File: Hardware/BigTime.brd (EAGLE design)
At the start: 43.2 x 43.2 mm, 14 parts, among them U1 ATMEGA328P_PDIP_EZ, Y1 32.768kHz

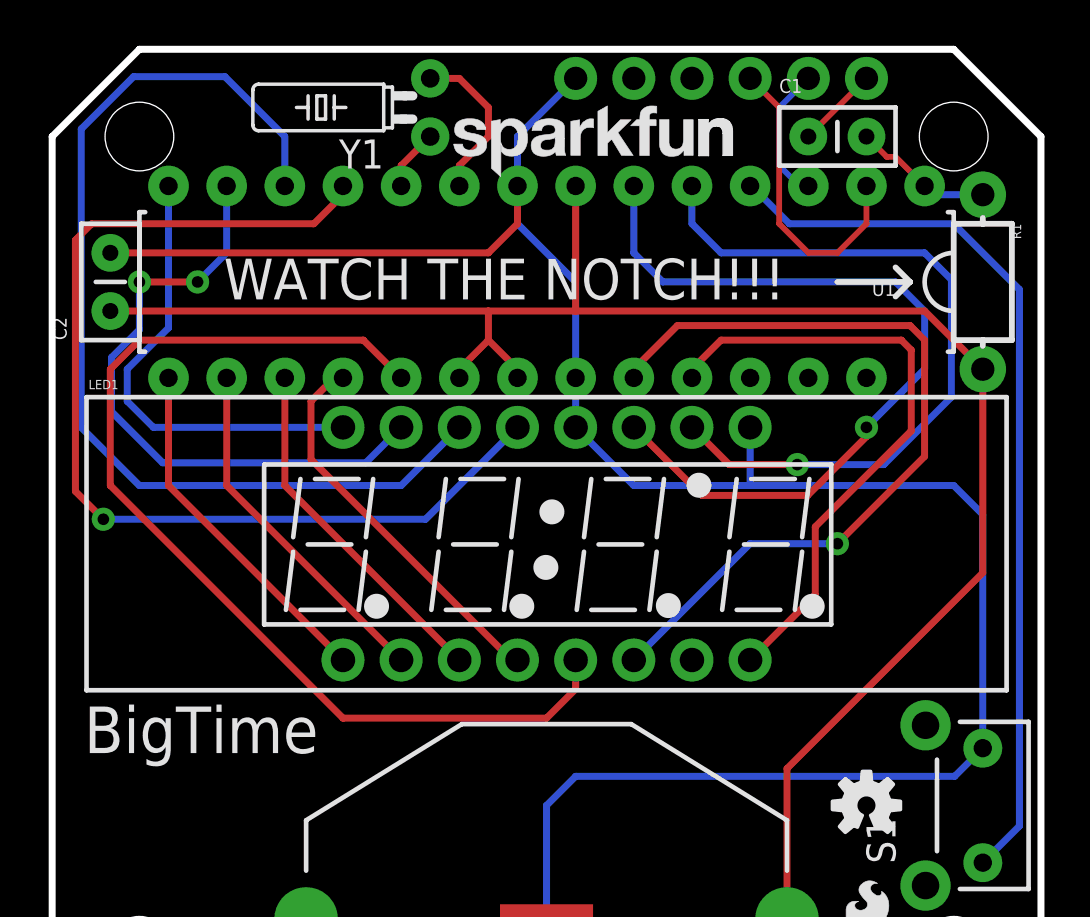
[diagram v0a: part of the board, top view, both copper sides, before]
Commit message: replace LED with bubble display
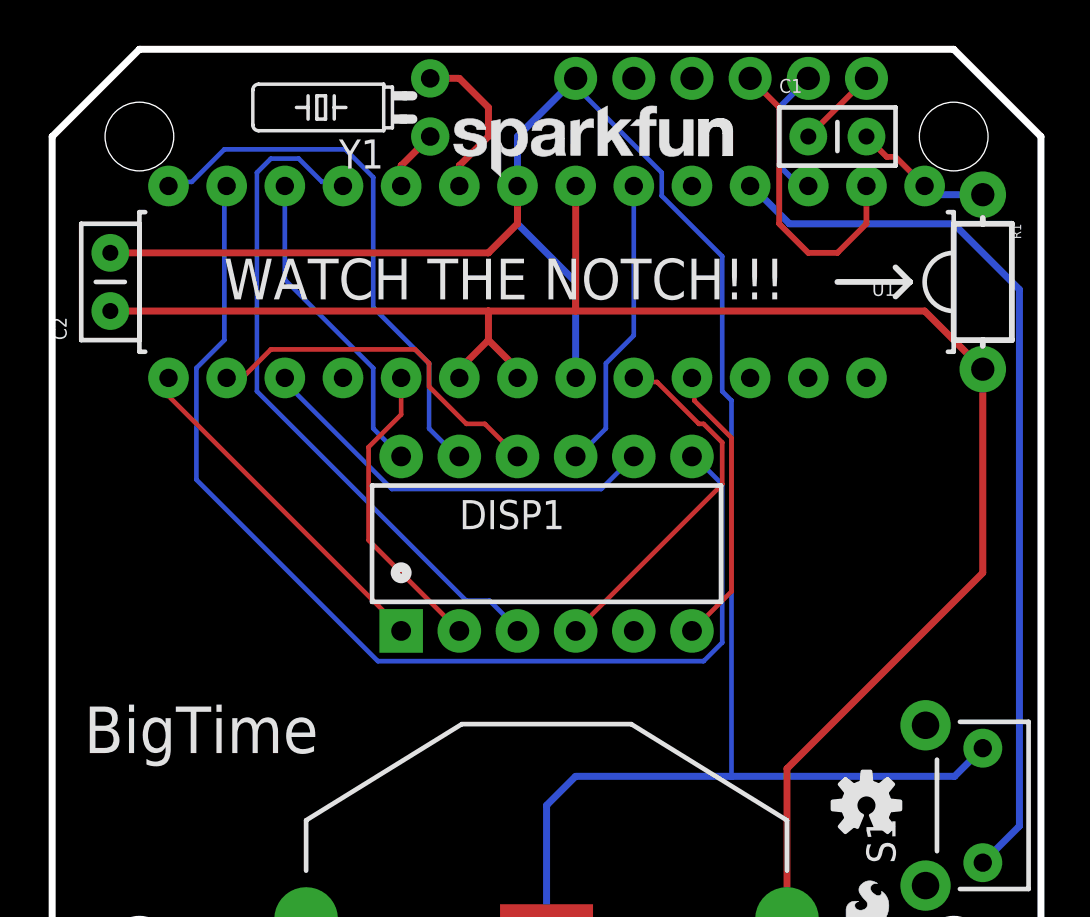
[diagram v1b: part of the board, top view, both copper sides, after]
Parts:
- removed LED1: 7-SEGMENT-4DIGIT-YOUNGSUNKIT, Testing:7-SEGMENT-4DIGIT-YOUNGSUN-KIT
- added DISP1: 7-SEGMENT-4DIGIT-COUNTER-HP-BUBBLE, SparkFun-Displays:DIL12
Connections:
- net A: now also DISP1.12; no longer LED1.14
- net AMPM: no longer LED1.10
- net B: now also DISP1.11; no longer LED1.16
- net C: now also DISP1.3; no longer LED1.13
- net COL: no longer LED1.4
- net D: now also DISP1.8; no longer LED1.3
- net DIG1: now also DISP1.1; no longer LED1.1
- net DIG2: now also DISP1.10; no longer LED1.2
- net DIG3: now also DISP1.4; no longer LED1.6
- net DIG4: now also DISP1.6; no longer LED1.8
- net DP: now also DISP1.5; no longer LED1.7
- net E: now also DISP1.2; no longer LED1.5
- net F: now also DISP1.9; no longer LED1.11
- net G: now also DISP1.7; no longer LED1.15
- net GND: no longer LED1.12, LED1.9
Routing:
- net AMPM: track 32.3 -> 0.00 mm, vias 1 -> 0
- net E: track 45.3 -> 13.3 mm
- net A: track 44.7 -> 13.9 mm
- net F: track 35.7 -> 12.9 mm, vias 1 -> 0
- net G: track 27.6 -> 48.7 mm, vias 2 -> 0
- net DIG3: track 35.6 -> 16.0 mm, vias 1 -> 0
- net COL: track 17.0 -> 0.00 mm
- net C: track 45.3 -> 29.9 mm, vias 1 -> 0
- net DIG4: track 27.1 -> 12.5 mm
- net B: track 20.0 -> 24.0 mm
- net D: track 15.5 -> 17.9 mm
- net GND: track 95.8 -> 95.0 mm

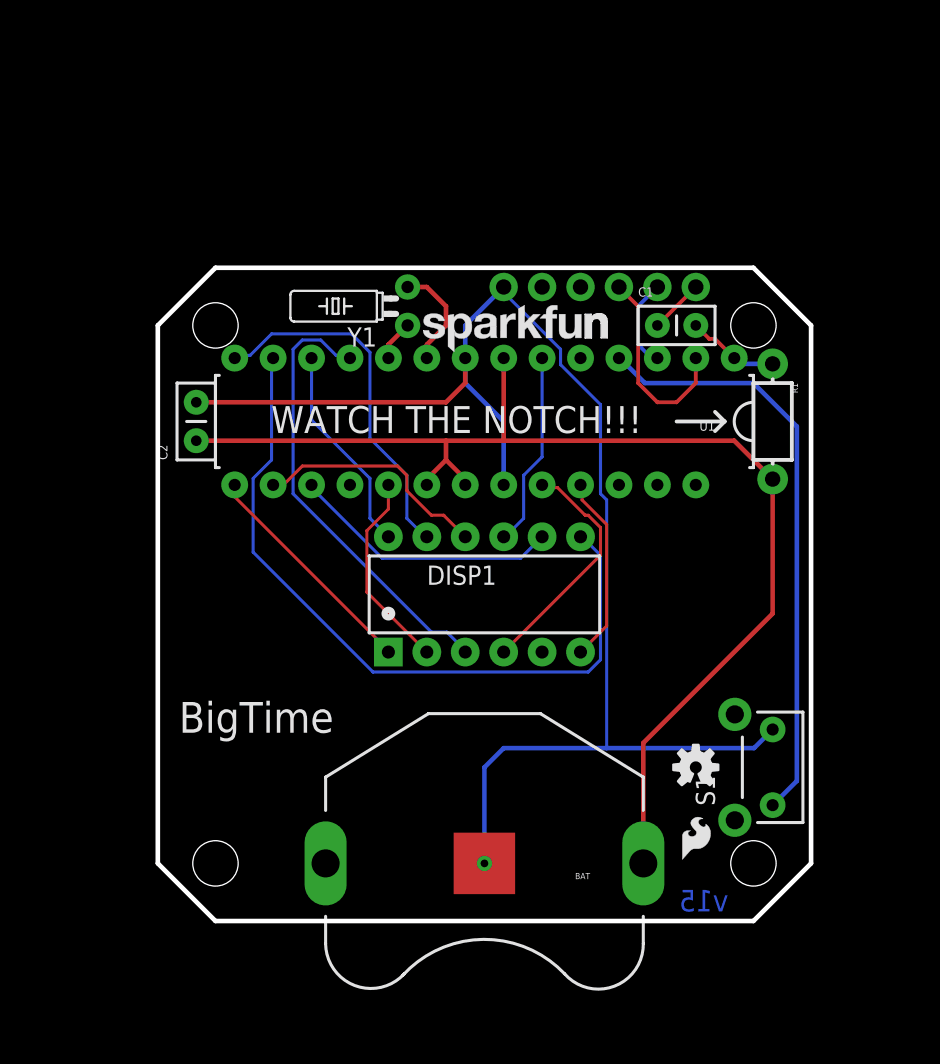
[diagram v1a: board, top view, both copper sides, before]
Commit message: add set button, reroute pub
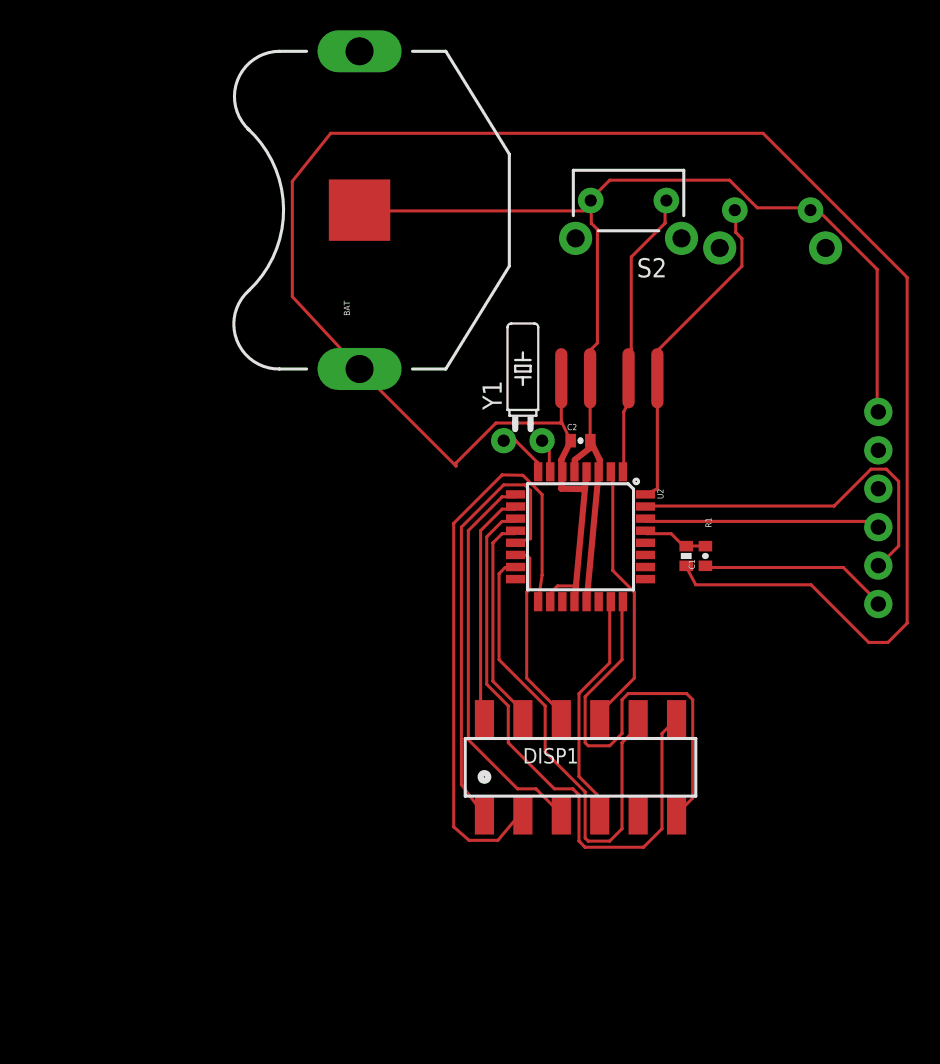
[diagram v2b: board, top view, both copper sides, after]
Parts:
- removed U$1: LOGO-SFESK, SparkFun:SFE-LOGO-FLAME
- removed U$3: LOGO-SFENEW, SparkFun:SFE-NEW-WEBLOGO
- removed U$4: OSHW-LOGOS, SparkFun:OSHW-LOGO-S
- removed U$5: LOGO-SFENW2, SparkFun:SFE-NEW-WEB
- removed U1: ATMEGA328P_PDIP_EZ, SparkFun-DigitalIC:DIL28-EZ
- added S2: BUTTON, SparkFun-Electromechanical:TACTILE-PTH-SIDEEZ
- added U2: ATMEGA328P_TQFP, SparkFun-DigitalIC:TQFP32-08
- C1, C2: device SparkFun-Passives:CAP-PTH-SMALLEZ -> SparkFun-Passives:0402-CAP
- DISP1: value 7-SEGMENT-4DIGIT-COUNTER-HP-BUBBLE -> 7-SEGMENT-4DIGIT-COUNTER-HP-BUBBLE-SM; device SparkFun-Displays:DIL12 -> SparkFun-Displays:DIL12_SM
- R1: device SparkFun-Passives:AXIAL-0.3-KIT -> SparkFun-Passives:0402-RES
- moved BAT 44.0 mm to (13.3, 47.0), turned to 90 degrees
- moved S1 36.8 mm to (40.6, 47.0), flipped to the bottom, turned to 180 degrees
- moved C2 25.4 mm to (27.9, 31.8), turned to 0 degrees
- moved JP1 24.2 mm to (47.6, 21.0), turned to 90 degrees
- moved C1 15.6 mm to (36.2, 24.1), turned to 90 degrees
- moved DISP1 13.1 mm to (27.9, 10.2)
- moved Y1 11.7 mm to (24.1, 31.8), turned to 0 degrees
- moved R1 10.6 mm to (34.9, 24.1)
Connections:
- removed net AMPM: U1.5
- new net SET: S2.1, U2.1
- net A: now also U2.10; no longer U1.12
- net B: now also U2.12; no longer U1.14
- net BTN: now also U2.32; no longer U1.4
- net C: now also U2.9; no longer U1.11
- net COL: now also U2.16; no longer U1.18
- net D: now also U2.15; no longer U1.17
- net DIG1: now also U2.13; no longer U1.15
- net DIG2: now also U2.14; no longer U1.16
- net DIG3: now also U2.23; no longer U1.23
- net DIG4: now also U2.24; no longer U1.24
- net E: now also U2.17; no longer U1.19
- net F: now also U2.2; no longer U1.6
- net G: now also U2.11; no longer U1.13
- net GND: now also S2.2, U2.21, U2.3, U2.5; no longer U1.22, U1.8
- net N$1: now also U2.8; no longer U1.10
- net N$2: now also U2.7; no longer U1.9
- net RST: now also R1.1, U2.29; no longer R1.P$1, U1.1
- net RXI: now also U2.30; no longer U1.2
- net TXO: now also U2.31; no longer U1.3
- net VCC: now also R1.2, U2.18, U2.20, U2.4, U2.6; no longer R1.P$2, U1.20, U1.21, U1.7
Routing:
- net VCC: track 79.2 -> 140.1 mm
- net E: track 13.3 -> 40.6 mm
- net SET: track 0.00 -> 19.0 mm
- net TXO: track 5.97 -> 24.2 mm
- net BTN: track 39.3 -> 21.8 mm
- net GND: track 95.0 -> 77.7 mm, vias 1 -> 0
- net DIG4: track 12.5 -> 28.5 mm
- net DIG1: track 15.3 -> 29.6 mm
- net D: track 17.9 -> 31.6 mm
- net B: track 24.0 -> 14.4 mm
- net G: track 48.7 -> 39.6 mm
- net N$3: track 3.59 -> 12.5 mm
- net F: track 12.9 -> 18.0 mm
- net N$2: track 7.02 -> 2.27 mm
- net C: track 29.9 -> 26.2 mm
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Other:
- board outline removed
- board text removed: "BLK"
- board text removed: "BigTime"
- board text removed: "Built on:"
- board text removed: "FTDI"
- board text removed: "GRN"
- board text removed: "WATCH THE NOTCH!!!"
- board text removed: "v15"

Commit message: more efficient pin arrangement
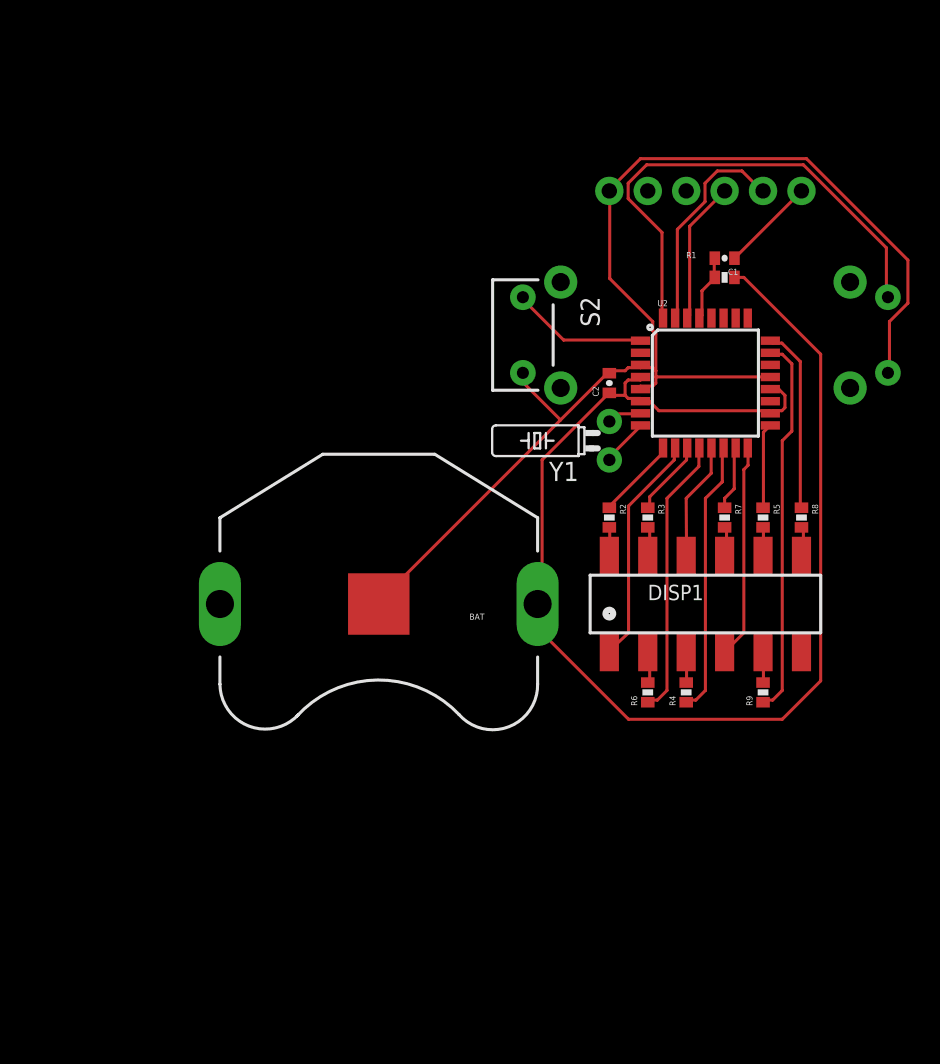
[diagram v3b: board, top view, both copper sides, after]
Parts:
- added R2, R3, R4, R5, R6, R7, R8, R9: 330, SparkFun-Passives:0402-RES
- moved JP1 27.8 mm to (42.5, 48.3), turned to 0 degrees
- moved BAT 26.1 mm to (14.6, 21.0), turned to 180 degrees
- moved C1 19.7 mm to (37.5, 43.8), turned to 180 degrees
- moved R1 18.6 mm to (37.5, 42.5), turned to 0 degrees
- moved DISP1 13.6 mm to (36.2, 21.0)
- moved U2 13.1 mm to (36.2, 35.6), turned to 0 degrees
- moved S2 11.3 mm to (24.1, 38.7), turned to 270 degrees
- moved S1 11.2 mm to (48.3, 38.7), turned to 270 degrees
- moved Y1 5.71 mm to (29.8, 31.8), turned to 90 degrees
- moved C2 4.26 mm to (29.8, 35.6), turned to 90 degrees
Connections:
- removed net COL: U2.16
- new net N$10: DISP1.7, R8.2
- new net N$11: DISP1.5, R9.2
- new net N$4: DISP1.12, R2.2
- new net N$5: DISP1.11, R3.2
- new net N$6: DISP1.3, R4.2
- new net N$7: DISP1.8, R5.2
- new net N$8: DISP1.2, R6.2
- new net N$9: DISP1.9, R7.2
- net A: now also R2.1, U2.9; no longer DISP1.12, U2.10
- net B: now also R3.1, U2.11; no longer DISP1.11, U2.12
- net C: now also R4.1, U2.14; no longer DISP1.3, U2.9
- net D: now also R5.1, U2.17; no longer DISP1.8, U2.15
- net DIG1: now also U2.10; no longer U2.13
- net DIG2: now also U2.13; no longer U2.14
- net DIG3: now also U2.16; no longer U2.23
- net DIG4: no longer U2.24
- net DP: now also R9.1, U2.23; no longer DISP1.5
- net E: now also R6.1, U2.12; no longer DISP1.2, U2.17
- net F: now also R7.1, U2.15; no longer DISP1.9, U2.2
- net G: now also R8.1, U2.24; no longer DISP1.7, U2.11
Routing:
- net VCC: track 140.1 -> 85.9 mm
- net DIG4: track 28.5 -> 0.00 mm
- net G: track 39.6 -> 12.2 mm
- net D: track 31.6 -> 5.63 mm
- net DP: track 0.00 -> 25.3 mm
- net E: track 40.6 -> 18.6 mm
- net DIG1: track 29.6 -> 15.3 mm
- net F: track 18.0 -> 4.24 mm
- net BTN: track 21.8 -> 33.1 mm
- net A: track 15.6 -> 5.51 mm
- net SET: track 19.0 -> 9.06 mm
- net TXO: track 24.2 -> 14.4 mm
- net B: track 14.4 -> 5.02 mm
- net C: track 26.2 -> 18.3 mm
- net RXI: track 15.7 -> 9.42 mm
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
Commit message: rearrange pins, start fitting to size
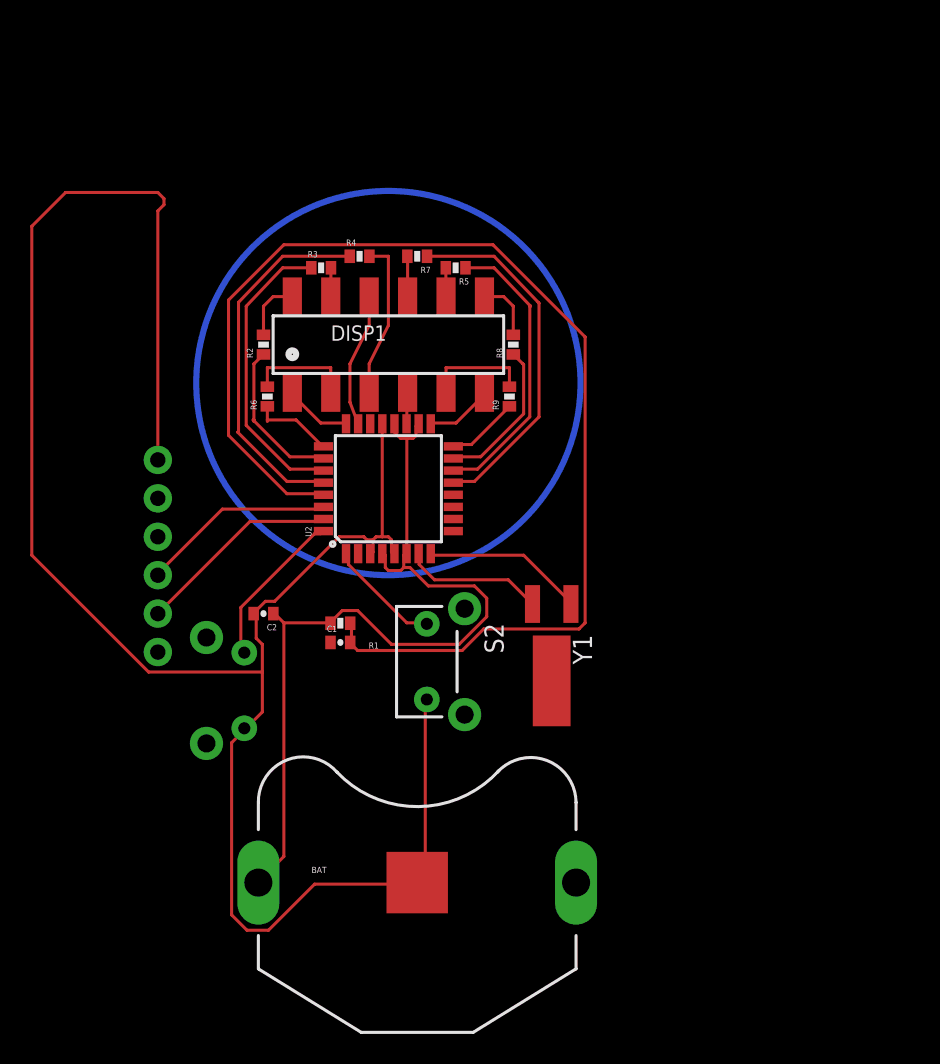
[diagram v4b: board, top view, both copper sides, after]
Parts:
- Y1: device SparkFun-FreqCtrl:TC26HEZ -> SparkFun-FreqCtrl:CRYSTAL-32KHZ-SMD
- moved JP1 52.3 mm to (0.00, 17.8), turned to 90 degrees
- moved S1 48.6 mm to (5.71, 15.2)
- moved R4 36.0 mm to (13.3, 43.9), turned to 0 degrees
- moved C1 35.9 mm to (12.1, 18.4), turned to 0 degrees
- moved R1 34.2 mm to (12.1, 19.7), turned to 180 degrees
- moved R6 31.9 mm to (7.24, 34.7)
- moved C2 27.5 mm to (6.99, 20.3), turned to 180 degrees
- moved R3 27.2 mm to (10.8, 43.2), turned to 0 degrees
- moved DISP1 27.1 mm to (15.2, 38.1)
- moved R7 26.7 mm to (17.1, 43.9), turned to 180 degrees
- moved R5 26.2 mm to (19.7, 43.2), turned to 180 degrees
- moved R9 25.8 mm to (23.2, 34.7)
- moved R2 25.6 mm to (6.99, 38.1), turned to 90 degrees
- moved S2 22.5 mm to (17.8, 17.1)
- moved R8 22.2 mm to (23.5, 38.1), turned to 90 degrees
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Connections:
- new net 5: U2.9
- new net 6: U2.10
- new net 7: U2.11
- new net 8: U2.12
- net A: now also U2.26; no longer U2.9
- net B: now also U2.27; no longer U2.11
- net C: now also U2.28; no longer U2.14
- net D: now also U2.14; no longer U2.17
- net DIG1: now also U2.24; no longer U2.10
- net DIG2: now also U2.23; no longer U2.13
- net DIG3: now also U2.19; no longer U2.16
- net DIG4: now also U2.17
- net DP: now also U2.16; no longer U2.23
- net E: now also U2.25; no longer U2.12
- net F: now also U2.13; no longer U2.15
- net G: now also U2.15; no longer U2.24
- net N$1: now also Y1.X1; no longer Y1.1
- net N$2: now also Y1.X2; no longer Y1.2
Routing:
- net RST: track 4.39 -> 81.2 mm
- net GND: track 83.6 -> 136.1 mm
- net VCC: track 85.9 -> 56.0 mm
- net BTN: track 33.1 -> 10.6 mm
- net DP: track 25.3 -> 4.79 mm
- net F: track 4.24 -> 23.7 mm
- net B: track 5.02 -> 19.6 mm
- net D: track 5.63 -> 19.3 mm
- net E: track 18.6 -> 5.42 mm
- net DIG3: track 14.1 -> 2.07 mm
- net DIG1: track 15.3 -> 4.46 mm
- net N$6: track 2.02 -> 10.6 mm
- net N$1: track 3.38 -> 10.7 mm
- net N$2: track 2.34 -> 9.29 mm
- net N$3: track 6.28 -> 0.00 mm
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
